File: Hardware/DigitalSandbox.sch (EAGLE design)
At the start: 82 parts, among them J1 AVR_SPI_PRG_6NS, Q1 MOSFET-N, Q2 MOSFET-P, Q3 MMBT2222A, Q4 MMBT2222A, Q5 MMBT2222A, U1 MCP73831, U10 LIGHTSENSORALS, U2 ATMEGA328, U3 C2031N-1A2-B10K-GP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

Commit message: corrected silk and moved vias to prevent ground plane breaks. Touched up layout of schematic to add tags and remove confusing junctions
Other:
- moved on the sheet: C1, C10, C11, C12, C13, C14, C2, C3, C4, C5, C6, C7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

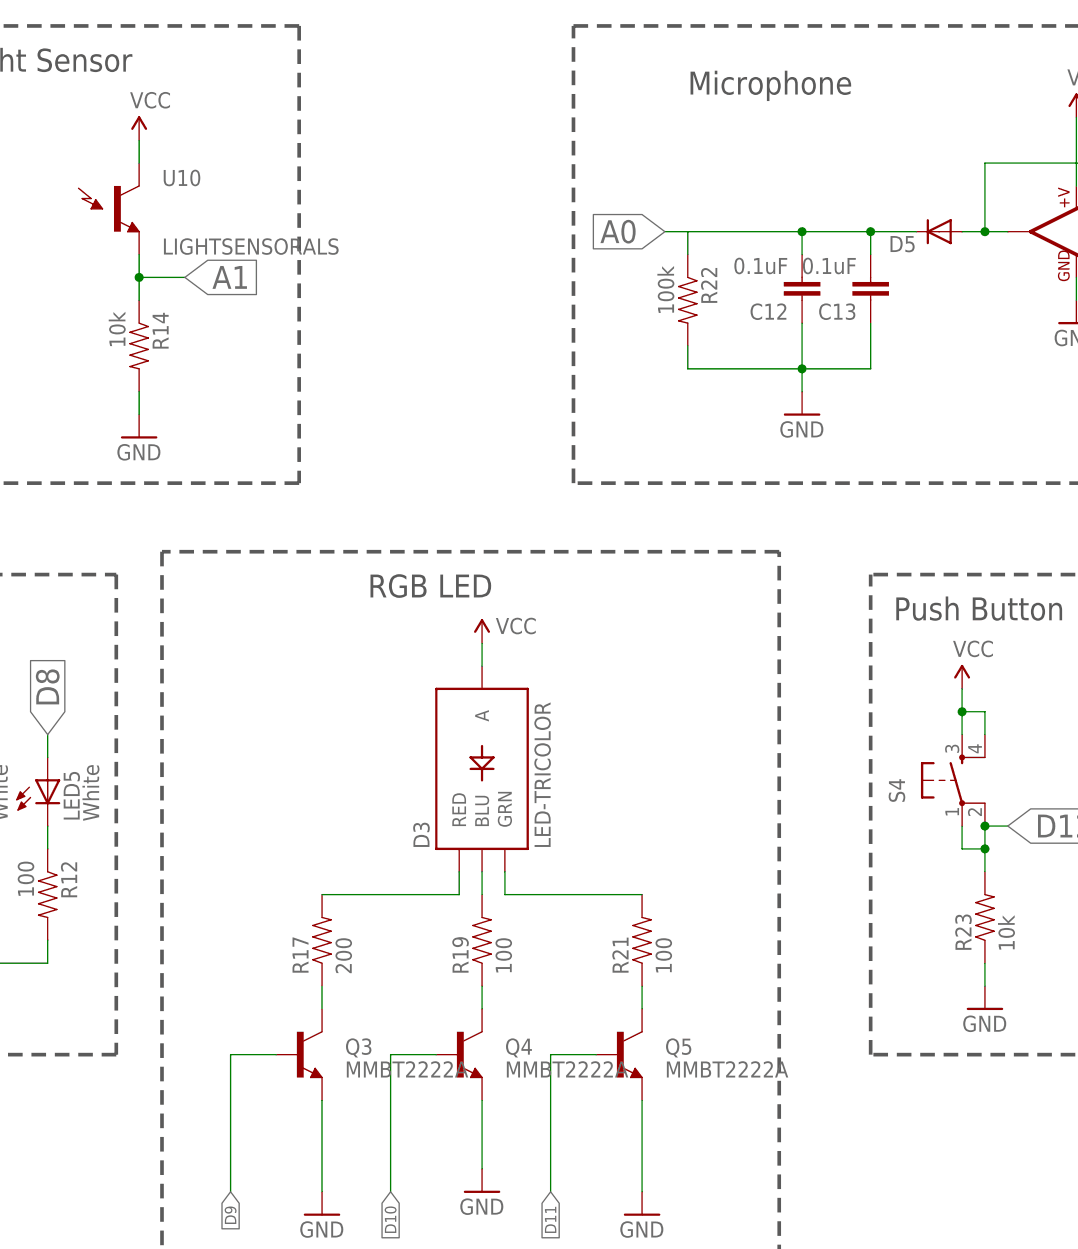
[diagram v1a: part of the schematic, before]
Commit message: modified Transistor names to reflect BOM I will add a new part the the LIB soon
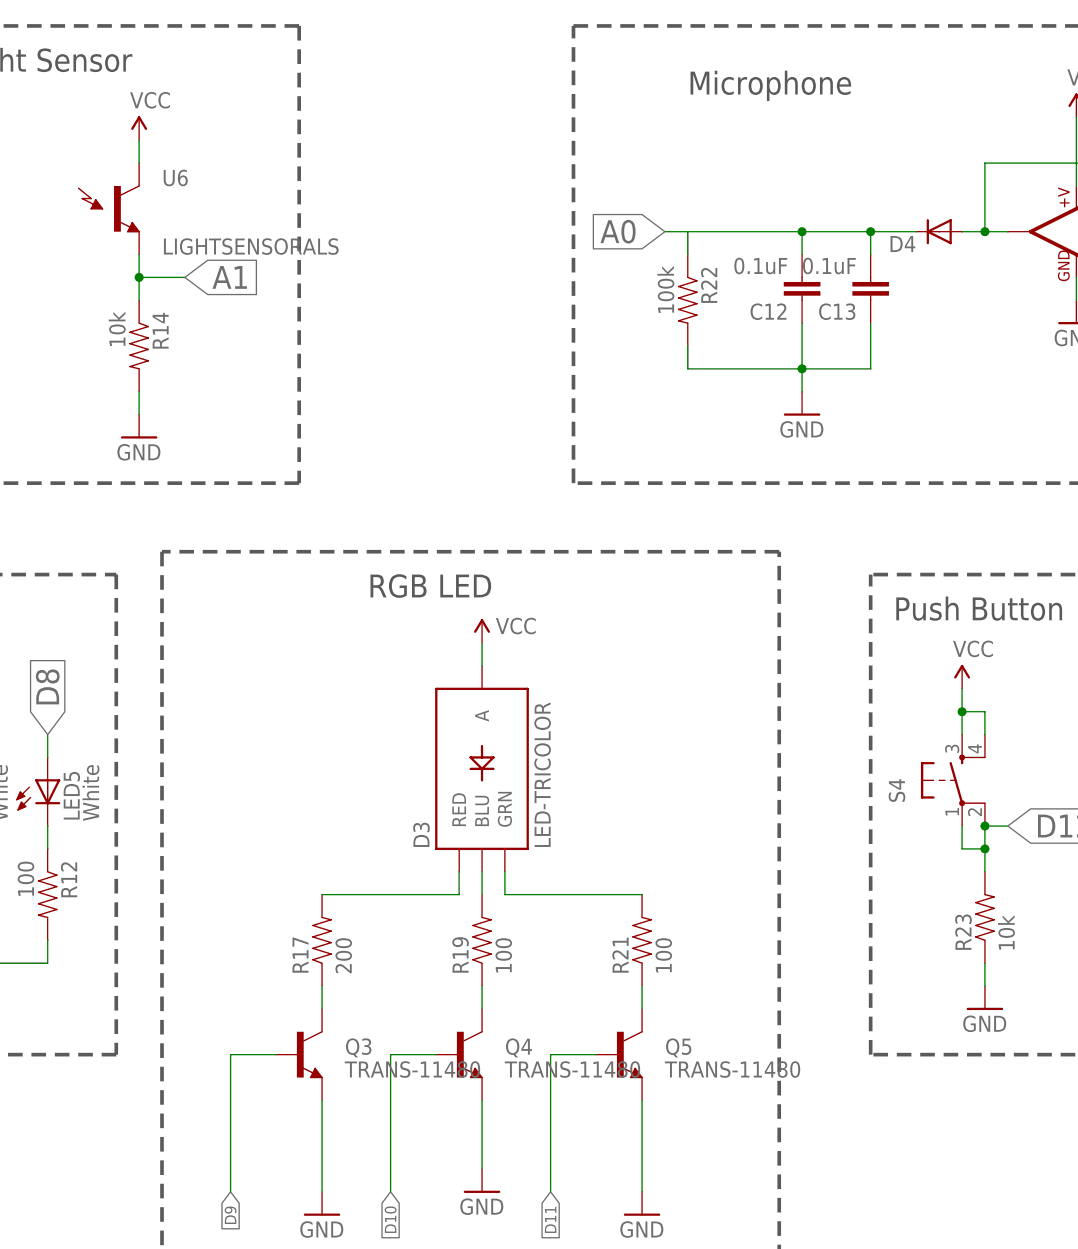
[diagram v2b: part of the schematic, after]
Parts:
- Q3, Q4, Q5: value MMBT2222A -> TRANS-11480
- renumbered D5 to D4, U10 to U6
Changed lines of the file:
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@@
 <part name="GND35" library="SparkFun" deviceset="GND" device=""/>
 <part name="GND36" library="SparkFun" deviceset="GND" device=""/>
-<part name="Q3" library="SparkFun-DiscreteSemi" deviceset="TRANSISTOR_NPN" device="MMBT2222A" value="MMBT2222A"/>
-<part name="Q4" library="SparkFun-DiscreteSemi" deviceset="TRANSISTOR_NPN" device="MMBT2222A" value="MMBT2222A"/>
-<part name="Q5" library="SparkFun-DiscreteSemi" deviceset="TRANSISTOR_NPN" device="MMBT2222A" value="MMBT2222A"/>
-<part name="U10" library="SparkFun-Sensors" deviceset="LIGHTSENSOR" device="ALS"/>
-<part name="D5" library="SparkFun-DiscreteSemi" deviceset="DIODE" device="SOD"/>
+<part name="Q3" library="SparkFun-DiscreteSemi" deviceset="TRANSISTOR_NPN" device="MMBT2222A" value="TRANS-11480"/>
+<part name="Q4" library="SparkFun-DiscreteSemi" deviceset="TRANSISTOR_NPN" device="MMBT2222A" value="TRANS-11480"/>
+<part name="Q5" library="SparkFun-DiscreteSemi" deviceset="TRANSISTOR_NPN" device="MMBT2222A" value="TRANS-11480"/>
+<part name="U6" library="SparkFun-Sensors" deviceset="LIGHTSENSOR" device="ALS"/>
+<part name="D4" library="SparkFun-DiscreteSemi" deviceset="DIODE" device="SOD"/>
 <part name="J1" library="SparkFun-Connectors" deviceset="AVR_SPI_PRG_6" device="NS"/>
 <part name="GND37" library="SparkFun" deviceset="GND" device=""/>
@@
 <instance part="Q4" gate="G$1" x="271.78" y="86.36"/>
 <instance part="Q5" gate="G$1" x="289.56" y="86.36"/>
-<instance part="U10" gate="G$1" x="233.68" y="180.34"/>
-<instance part="D5" gate="G$1" x="325.12" y="177.8" rot="R180"/>
+<instance part="U6" gate="G$1" x="233.68" y="180.34"/>
+<instance part="D4" gate="G$1" x="325.12" y="177.8" rot="R180"/>
 <instance part="J1" gate="G$1" x="27.94" y="104.14"/>
 <instance part="GND37" gate="1" x="43.18" y="91.44"/>
@@
 <wire x1="236.22" y1="187.96" x2="236.22" y2="185.42" width="0.1524" layer="91"/>
 <pinref part="P+14" gate="1" pin="VCC"/>
-<pinref part="U10" gate="G$1" pin="C1"/>
+<pinref part="U6" gate="G$1" pin="C1"/>
 </segment>
 <segment>
@@
 <wire x1="297.18" y1="177.8" x2="294.64" y2="177.8" width="0.1524" layer="91"/>
 <label x="294.64" y="177.8" size="2.54" layer="95" rot="R180" xref="yes"/>
-<pinref part="D5" gate="G$1" pin="C"/>
+<pinref part="D4" gate="G$1" pin="C"/>
 </segment>
 </net>
@@
 <pinref part="R14" gate="G$1" pin="1"/>
 <label x="241.3" y="172.72" size="2.54" layer="95" xref="yes"/>
-<pinref part="U10" gate="G$1" pin="E1"/>
+<pinref part="U6" gate="G$1" pin="E1"/>
 </segment>
 </net>
@@
 <pinref part="U8" gate="G$1" pin="-IN1"/>
 <pinref part="U8" gate="G$1" pin="OUT1"/>
-<pinref part="D5" gate="G$1" pin="A"/>
-</segment>
-</net>
+<pinref part="D4" gate="G$1" pin="A"/>
+</segment>
+</net>

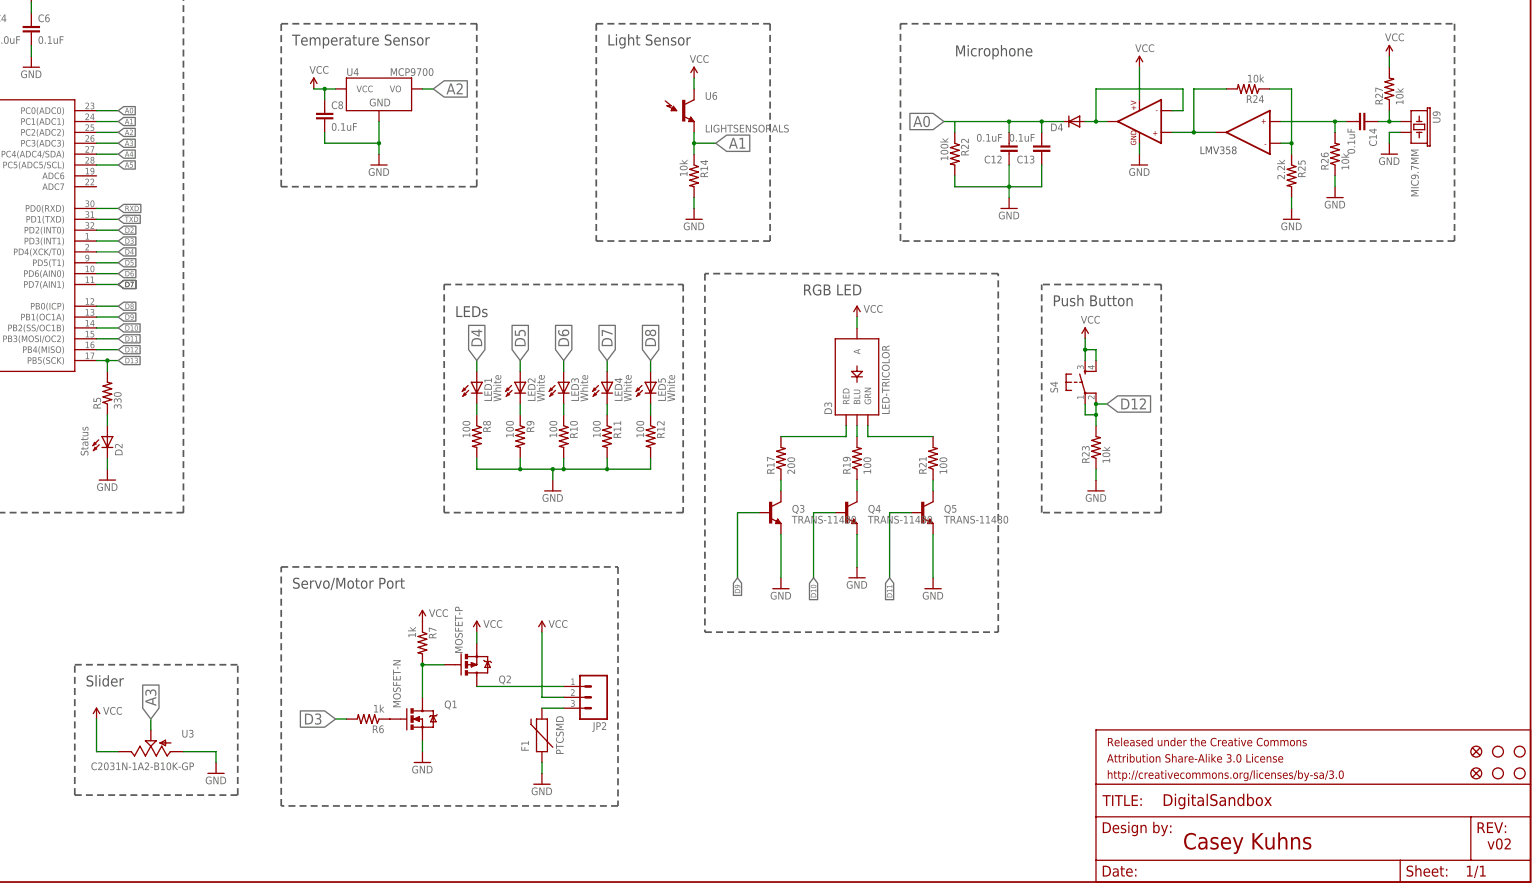
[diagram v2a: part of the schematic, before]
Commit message: Completed:
1. D13 led from 0603 yellow to 1206 Red.
2. Re-order A0 - A2.
3. Add Flyback diode on Motor port
4. Change resistor values on LED row to 330ohm to reduce intensity.
6. Label D3 output for motors and servos
7. Replace D12 pushbutton with new raised head button.
8. replace RGB LED with one spec'ed by Nate.
9. Re-order LED pins on Silk.

TODO:
5. Investigate the Microphone circuit to increase output.
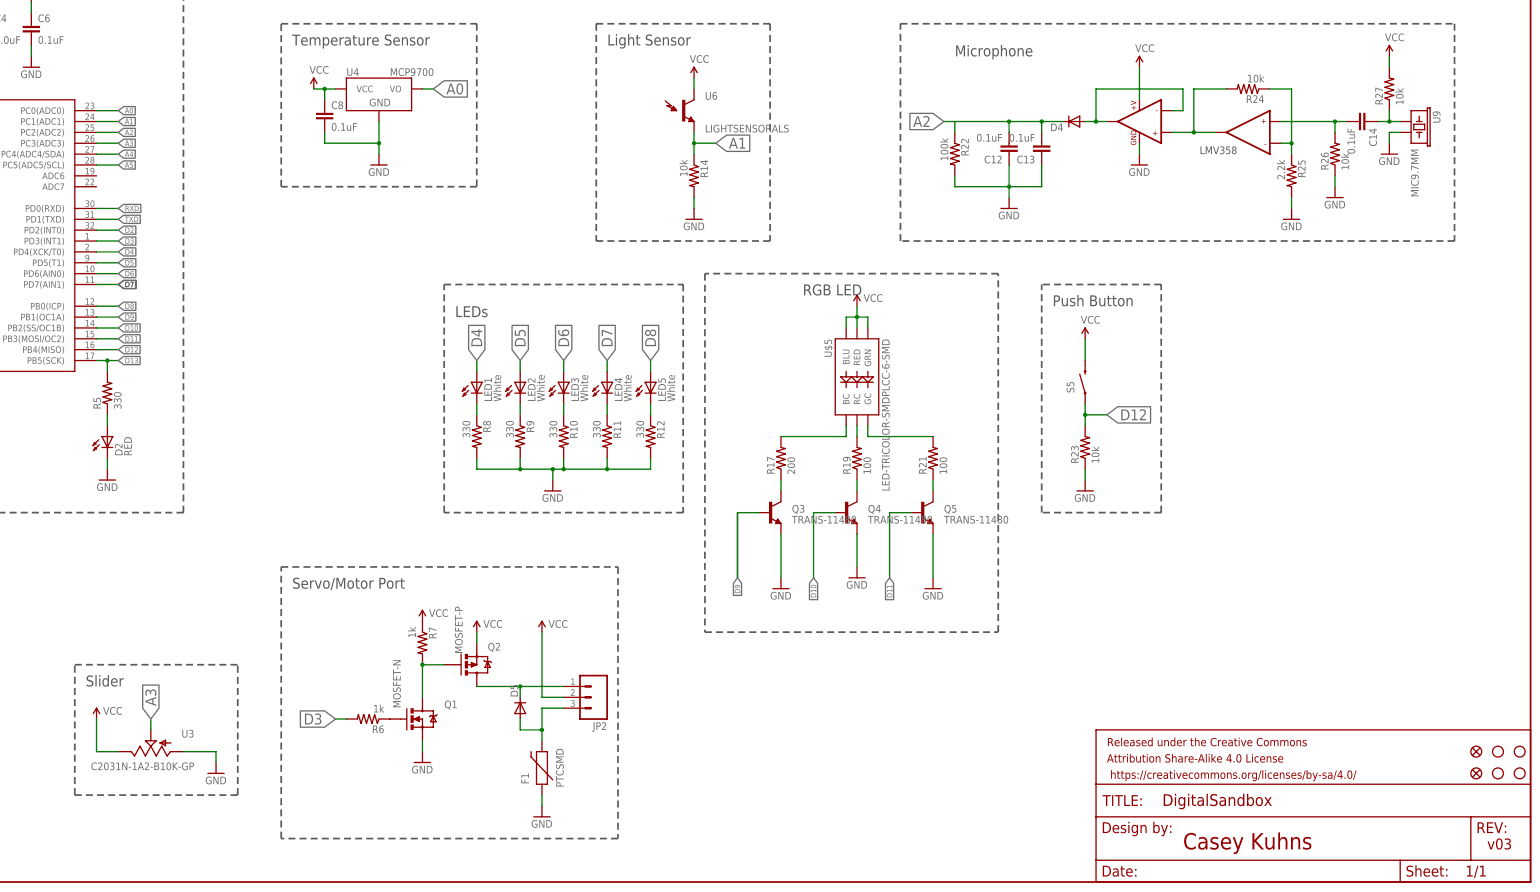
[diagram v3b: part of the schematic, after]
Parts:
- removed D3: LED-TRICOLOR, SparkFun:LED-TRICOLOR
- removed S4: (no value), SparkFun:TAC_SWITCHSMD
- added D5: (no value), SparkFun-DiscreteSemi:DIODESOD
- added S5: SWITCH-MOMENTARY-2SMD-4, SparkFun-Electromechanical:SWITCH-MOMENTARY-2SMD-4
- added U$5: LED-TRICOLOR-SMDPLCC-6-SMD, Testing:LED-TRICOLOR-SMDPLCC-6-SMD
- D2: value Status -> RED; device SparkFun:LED0603 -> SparkFun-LED:LED-RED1206
- R10, R11, R12, R8, R9: value 100 -> 330; device SparkFun-Passives:RESISTOR0603-RES -> SparkFun-Resistors:33OHM1/10W1%(0603)
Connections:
- net A0: now also U4.VO; no longer C12.2, C13.2, D4.C, R22.1
- net A2: now also C12.2, C13.2, D4.C, R22.1; no longer U4.VO
- net D12: now also S5.1; no longer S4.1, S4.2
- net GRN: now also U$5.GC; no longer D3.GRN
- net N$16: now also D5.A
- net N$28: now also U$5.RC; no longer D3.BLU
- net N$8: now also D5.C
- net RED: now also U$5.BC; no longer D3.RED
- net VCC: now also S5.2, U$5.BLU, U$5.GRN, U$5.RED; no longer D3.A, S4.3, S4.4
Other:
- note added: "v03"
- note removed: "v02"
- moved on the sheet: F1, R23

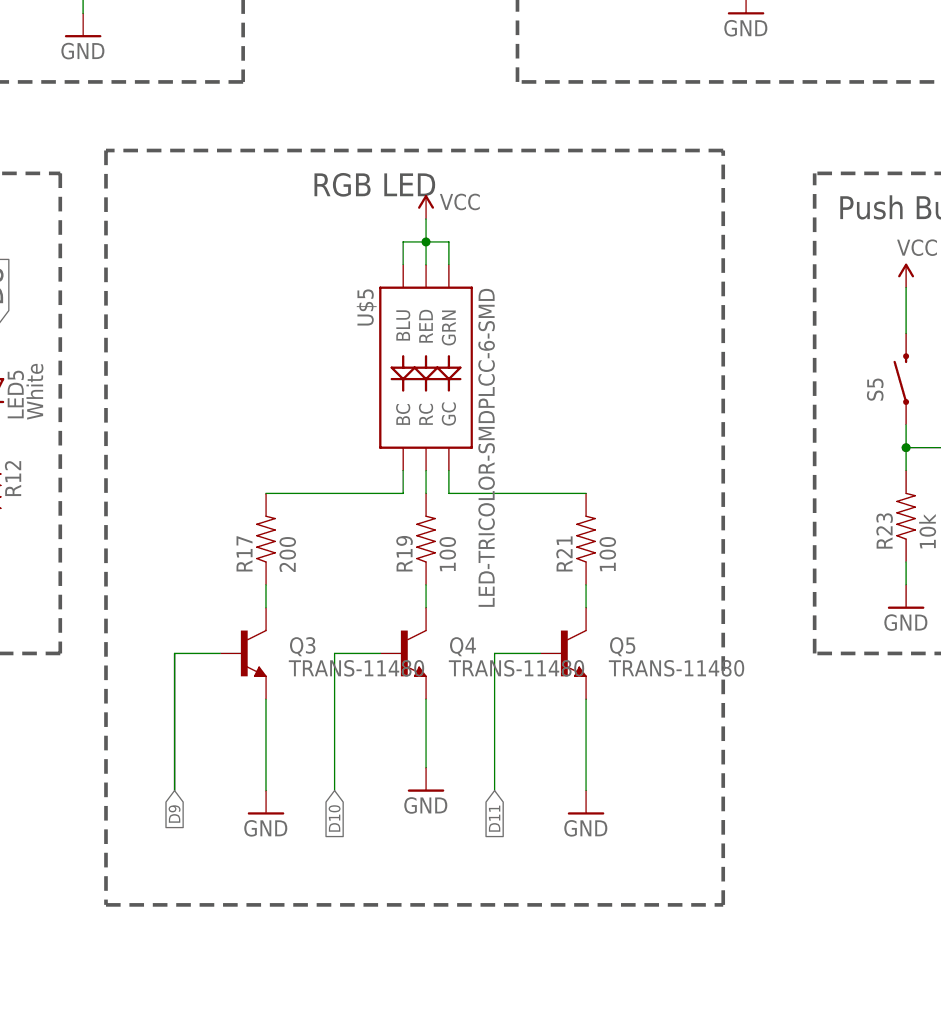
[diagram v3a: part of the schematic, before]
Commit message: removed power transistors from RGB LED's.
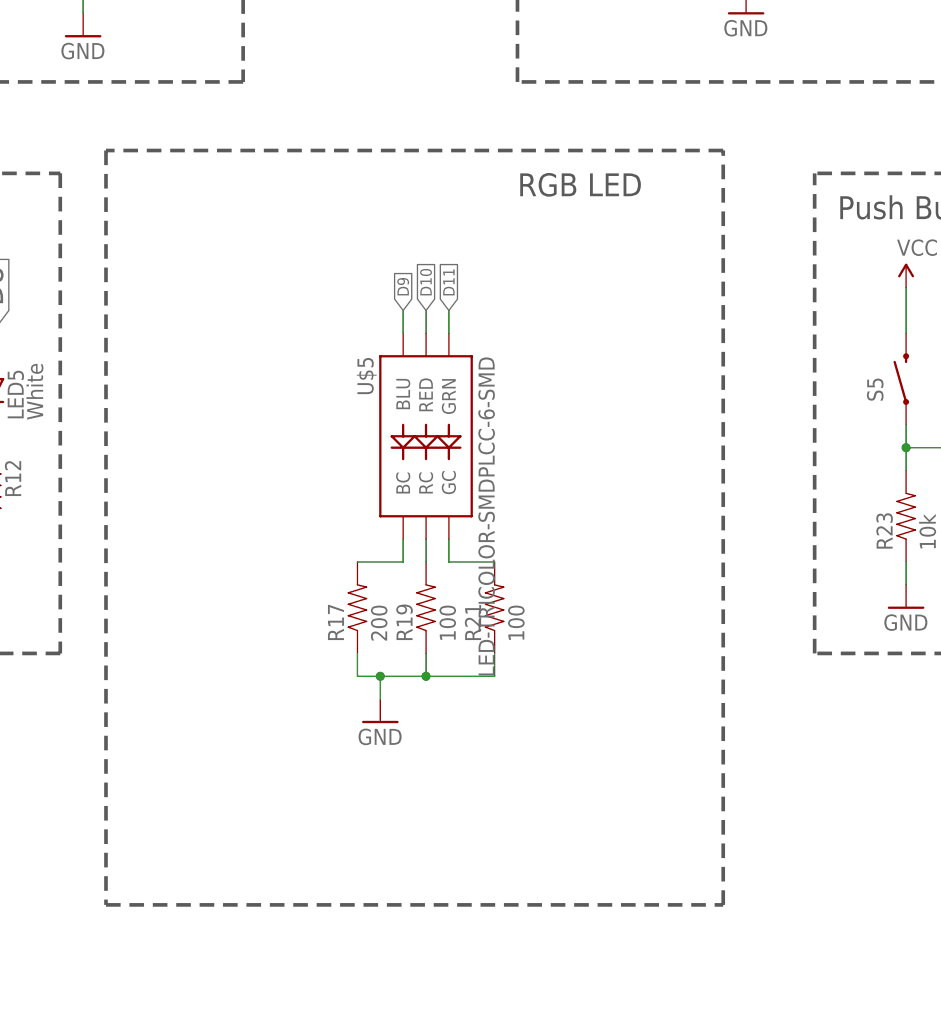
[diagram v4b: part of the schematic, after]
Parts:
- removed Q3, Q4, Q5: TRANS-11480, SparkFun-DiscreteSemi:TRANSISTOR_NPNMMBT2222A
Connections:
- removed net N$25: Q5.C, R21.1
- removed net N$27: Q4.C, R19.1
- removed net N$29: Q3.C, R17.1
- net D10: now also U$5.RED; no longer Q4.B
- net D11: now also U$5.GRN; no longer Q5.B
- net D9: now also U$5.BLU; no longer Q3.B
- net GND: now also R17.1, R19.1, R21.1; no longer Q3.E, Q4.E, Q5.E
- net VCC: no longer U$5.BLU, U$5.GRN, U$5.RED
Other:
- moved on the sheet: R17, R19, R21, U$5

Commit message: added Rev number
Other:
- note added: "v10"
- note removed: "v03"
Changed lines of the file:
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@@
 <wire x1="345.44" y1="86.36" x2="345.44" y2="139.7" width="0.4064" layer="97" style="shortdash"/>
 <wire x1="345.44" y1="86.36" x2="317.5" y2="86.36" width="0.4064" layer="97" style="shortdash"/>
-<text x="421.64" y="7.62" size="2.54" layer="94" font="vector">v03</text>
+<text x="421.64" y="7.62" size="2.54" layer="94" font="vector">v10</text>
 </plain>
 <instances>
